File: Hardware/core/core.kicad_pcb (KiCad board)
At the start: 4 copper layers, 31.3 x 67.7 mm, 32 parts, among them J17 PROG, J18 USB_C_Receptacle_USB2.0_14P, J5 TO_NEXT, J7 TO_NEXT, J8 Conn_02x09_Odd_Even, SW1 RESET, SW2 BOOT, U10 SN74AHCT1G14DCKR, U19 ESP32-S3-MINI-1, U20 AP2112K-3.3TRG1, U21 SN65HVD230DR

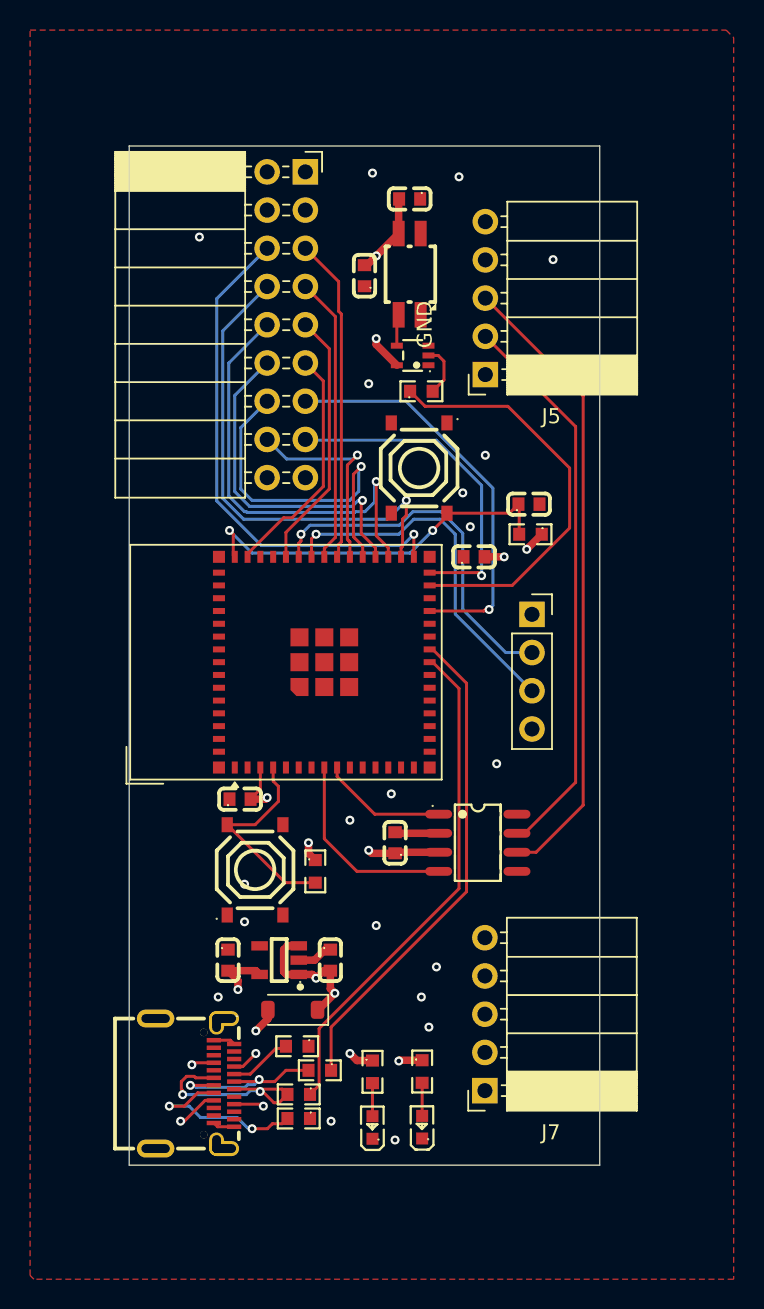
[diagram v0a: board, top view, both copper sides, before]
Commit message: Flatten Core and Backbone KiCad project paths
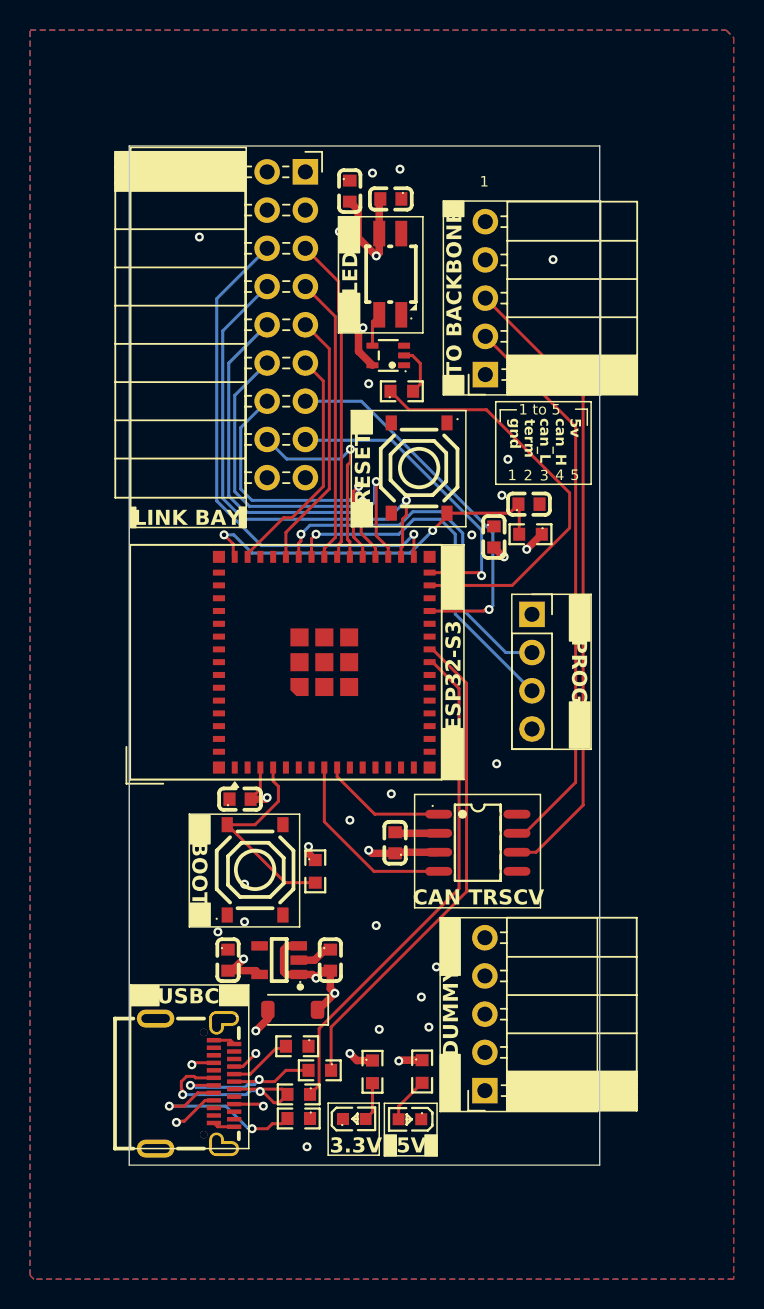
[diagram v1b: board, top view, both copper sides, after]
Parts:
- moved C14 5.70 mm to (81.7, 70.7), turned to -90 degrees
- moved C75 1.87 mm to (91.3, 93.7), turned to -90 degrees
- moved U10 1.62 mm to (84.3, 81.6)
- moved D2 1.34 mm to (82.0, 132.4), turned to 0 degrees
- moved R10 1.30 mm to (85.2, 84.0)
- moved LED2 1.29 mm to (84.4, 76.2)
- moved C24 1.25 mm to (84.5, 71.2)
- moved D3 0.97 mm to (85.7, 132.4), turned to 180 degrees
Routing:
- net 5V: track 18.6 -> 22.1 mm
- net IO39: track 23.1 -> 20.4 mm
- net IO48: track 22.5 -> 20.8 mm
- net IO47: track 27.0 -> 25.3 mm
- net Net-(D3-A): track 2.20 -> 3.21 mm
- net VCORE: track 17.8 -> 17.1 mm
- net CORE_CAN_RX: track 13.2 -> 12.6 mm
- net GND: track 8.33 -> 8.61 mm, vias 20 -> 21
- added copper zone on B.Cu, net GND
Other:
- board text added: "1"
- board text added: "1 to 5"
- board text added: "2"
- board text added: "3"
- board text added: "3.3V"
- board text added: "4"
- board text added: "5"
- board text added: "5V"
- board text added: "5v"
- board text added: "BOOT"
- board text added: "CAN TRSCV"
- board text added: "DUMMY"
- board text added: "ESP32-S3"
- board text added: "LED"
- board text added: "LINK BAY"
- board text added: "PROG"
- board text added: "RESET"
- board text added: "TO BACKBONE"
- board text added: "USBC"
- board text added: "can_H"
- board text added: "can_L"
- board text added: "gnd"
- board text added: "term"

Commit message: Update Core PCB
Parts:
- moved J18 1.40 mm to (71.8, 128.7)
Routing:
- net GND: track 8.61 -> 13.1 mm, vias 21 -> 26
- net Net-(J18-D+-PadA6): track 11.7 -> 13.2 mm
- net Net-(J18-CC2): track 12.1 -> 13.0 mm
- net Net-(J18-CC1): track 4.21 -> 3.65 mm
- net VBUS: track 10.1 -> 10.5 mm, vias 5 -> 4
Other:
- outline, holes or cut-outs redrawn
